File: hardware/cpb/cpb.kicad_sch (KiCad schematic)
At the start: 132 parts, among them J1 Spacecraft Bus Stacking Conne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, J10 SW1, J11 SW2, J12 SW3, J13 PISW1, J14 μSW1, J15 μSW2, J16 μSW3, J17 μSW4, J2 I2CExt, J3 DAC1BUF, J4 DAC2BUF, J6 Raspberry Pi Zero 2W, J7 ADC6/7, J8 ADC2/3, J9 4FBRG, J99 RBFJUMP, Q1 PMBT2222A, Q2 IRF9393, Q3 MBT2222ADW1T1, Q4 PMBT2222A, U1 TS912, U2 ADR420ARMZ, U3 KF33BDT, U4 STM32L072R_B-Z_Tx, U5 AP62301WU, U6 SC16IS750xBS, Y1 14.7456MHz

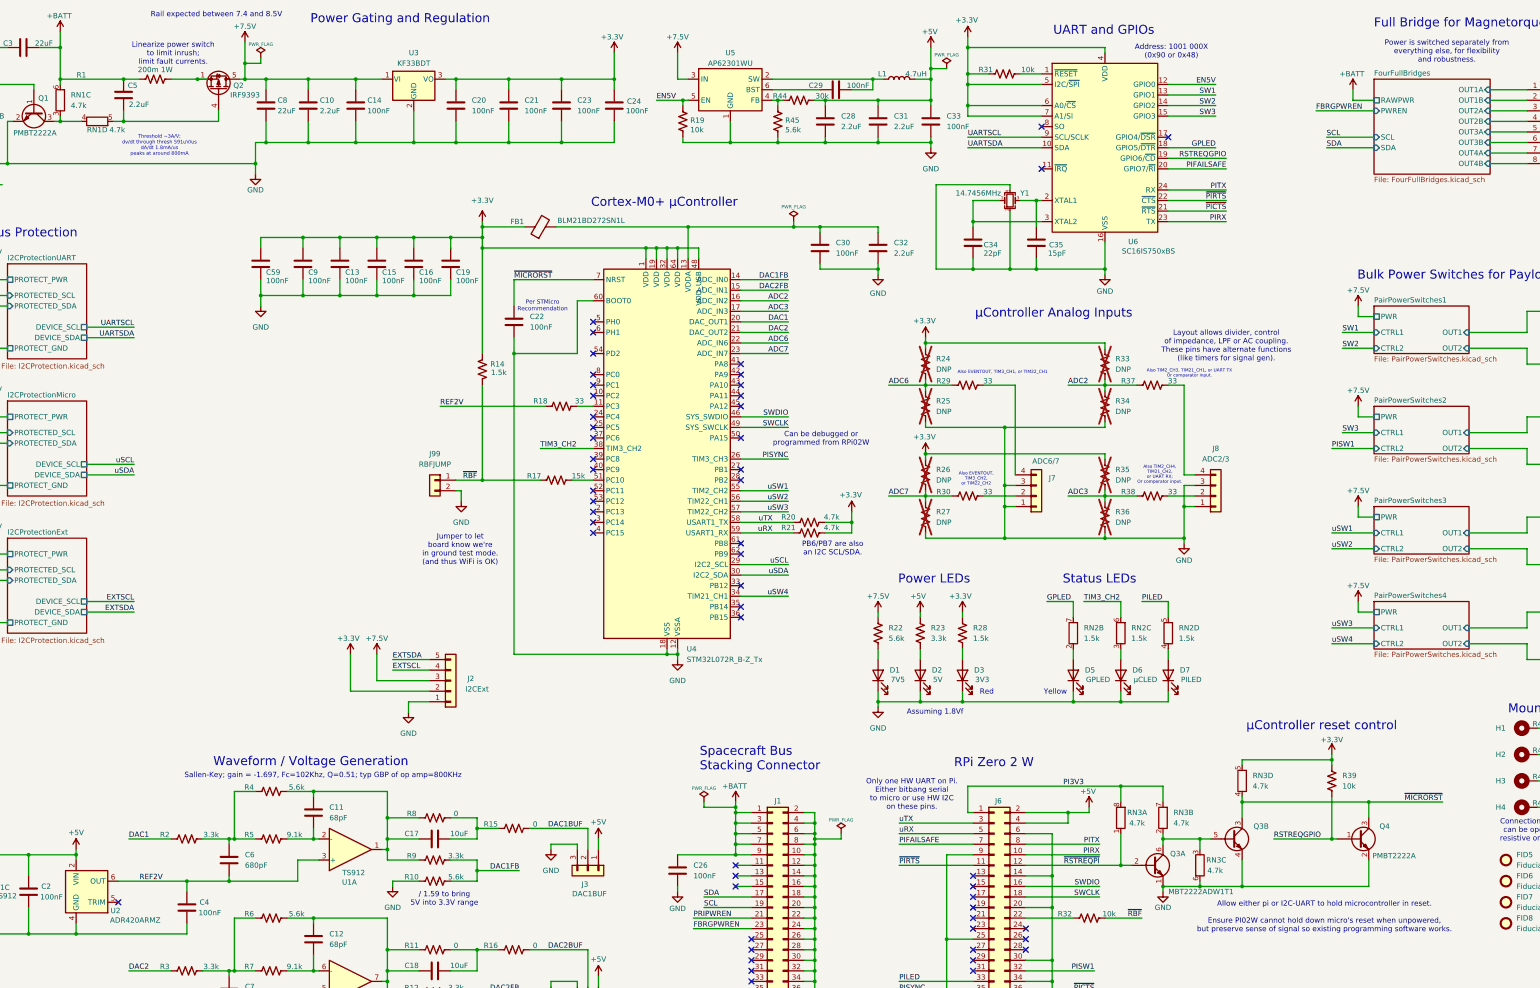
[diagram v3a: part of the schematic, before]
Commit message: hardware/cpb: finished revisions
did all things specified on Errata file for cpb;
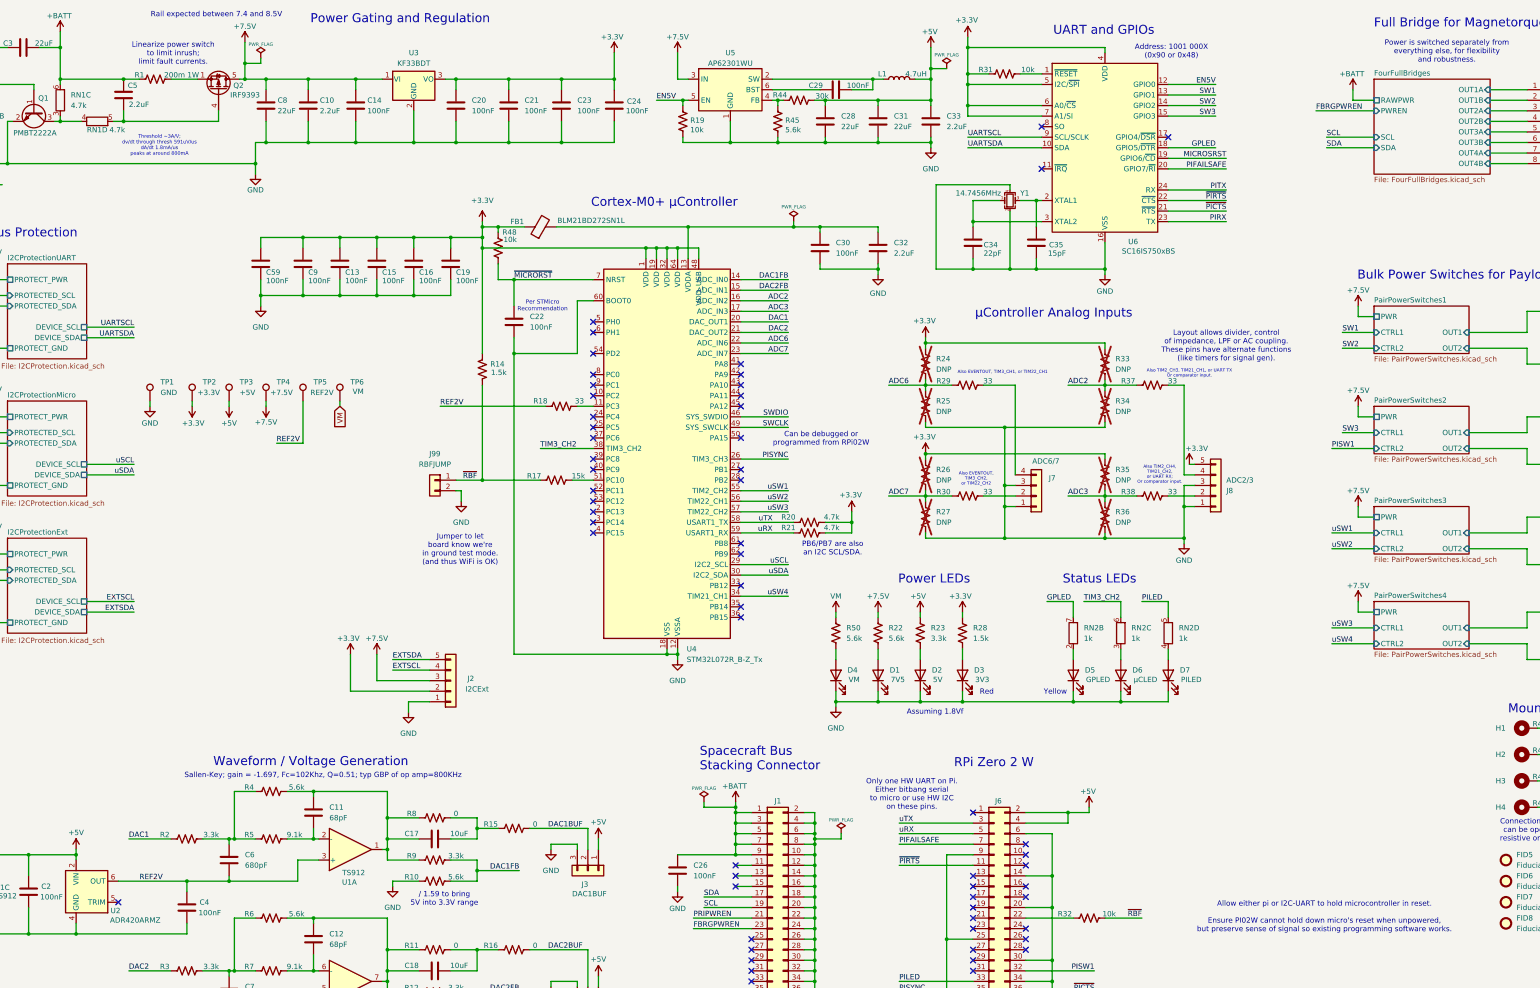
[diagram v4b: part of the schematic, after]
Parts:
- removed J8: ADC2/3, Connector_JST:JST_PH_B4B-PH-K_1x04_P2.00mm_Vertical, symbol Connector_Generic:Conn_01x04
- removed Q3: MBT2222ADW1T1, Package_TO_SOT_SMD:SOT-363_SC-70-6, symbol Transistor_BJT:MBT2222ADW1T1
- removed Q4: PMBT2222A, Package_TO_SOT_SMD:SOT-23, symbol Transistor_BJT:PMBT2222A
- removed R39: 10k, Resistor_SMD:R_0603_1608Metric, symbol Device:R_US
- removed RN3: 4.7k, Resistor_SMD:R_Array_Convex_4x0603, symbol Device:R_Pack04_Split
- added D4: VM, LED_SMD:LED_0805_2012Metric, symbol Device:LED
- added J8: ADC2/3, symbol Connector_Generic:Conn_01x05
- added R48: 10k, symbol Device:R_US
- added R50: 5.6k, Resistor_SMD:R_0603_1608Metric, symbol Device:R_US
- added TP1: GND, TestPoint:TestPoint_Keystone_5010-5014_Multipurpose, symbol Connector:TestPoint
- added TP2: +3.3V, TestPoint:TestPoint_Keystone_5010-5014_Multipurpose, symbol Connector:TestPoint
- added TP3: +5V, TestPoint:TestPoint_Keystone_5010-5014_Multipurpose, symbol Connector:TestPoint
- added TP4: +7.5V, TestPoint:TestPoint_Keystone_5010-5014_Multipurpose, symbol Connector:TestPoint
- added TP5: REF2V, TestPoint:TestPoint_Keystone_5010-5014_Multipurpose, symbol Connector:TestPoint
- added TP6: VM, TestPoint:TestPoint_Keystone_5010-5014_Multipurpose, symbol Connector:TestPoint
- C28, C31: value 2.2uF -> 22uF; LCSC C77047 -> C2178186
- C33: value 100nF -> 2.2uF; LCSC C77055 -> C77047
- RN2: value 1.5k -> 1k; LCSC C723702 -> C22548
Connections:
- net +3.3V: now also J8.5 (Pin_5), R48.1, TP2.1
- net +5V: now also TP3.1
- net +7.5V: now also TP4.1
- net GND: now also D4.1 (K), J8.1 (Pin_1), J8.3 (Pin_3), TP1.1
- net PIRX: no longer J6.10 (Pin_10)
- net PITX: no longer J6.8 (Pin_8)
- net REF2V: now also TP5.1
- net SWCLK: no longer J6.18 (Pin_18)
- net SWDIO: no longer J6.16 (Pin_16)
- net ~{MICRORST}: now also R48.2
- net at R38.2: now also J8.2 (Pin_2)
- net at R37.2: now also J8.4 (Pin_4)
- net PI3V3: no longer names the net of J6.1 (Pin_1)
- net RSTREQGPIO renamed MICROSRST
- net ~{RSTREQPI}: no longer names the net of J6.12 (Pin_12)
- new net: D4.2 (A), R50.2
- new net VM: R50.1, TP6.1
- no-connect marks 57 -> 63
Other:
- note removed: "μController reset control"

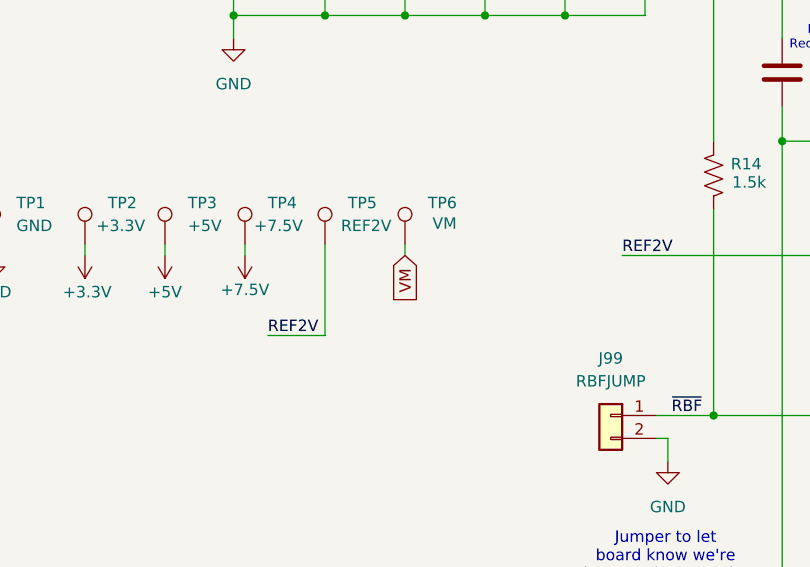
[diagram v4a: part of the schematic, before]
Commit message: hardware/cpb: changed labels, spread out components
changed vm labels, spread out somponents on Four Full Bridges sch;
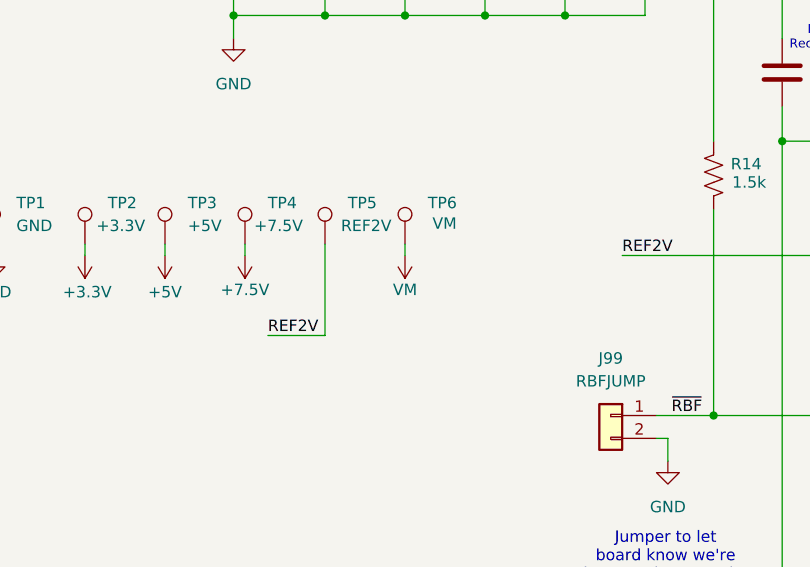
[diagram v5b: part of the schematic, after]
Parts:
- R48: footprint (none) -> Resistor_SMD:R_0603_1608Metric
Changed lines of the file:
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@@
 		)
 	)
-	(global_label "VM"
-		(shape input)
-		(at 111.76 107.95 270)
-		(fields_autoplaced yes)
-		(effects
-			(font
-				(size 1.27 1.27)
-			)
-			(justify right)
-		)
-		(property "Intersheetrefs" "${INTERSHEET_REFS}"
-			(at 111.76 113.4752 90)
-			(effects
-				(font
-					(size 1.27 1.27)
-				)
-				(justify right)
-				(hide yes)
-			)
-		)
-	)
 	(symbol
 		(lib_id "Device:C")
@@
 	)
 	(symbol
+		(lib_id "power:+7.5V")
+		(at 111.76 107.95 180)
+		(unit 1)
+		(exclude_from_sim no)
+		(in_bom yes)
+		(on_board yes)
+		(dnp no)
+		(property "Reference" "#PWR081"
+			(at 111.76 104.14 0)
+			(effects
+				(font
+					(size 1.27 1.27)
+				)
+				(hide yes)
+			)
+		)
+		(property "Value" "VM"
+			(at 111.76 111.76 0)
+			(effects
+				(font
+					(size 1.27 1.27)
+				)
+			)
+		)
+		(property "Footprint" ""
+			(at 111.76 107.95 0)
+			(effects
+				(font
+					(size 1.27 1.27)
+				)
+				(hide yes)
+			)
+		)
+		(property "Datasheet" ""
+			(at 111.76 107.95 0)
+			(effects
+				(font
+					(size 1.27 1.27)
+				)
+				(hide yes)
+			)
+		)
+		(property "Description" "Power symbol creates a global label with name \"+7.5V\""
+			(at 111.76 107.95 0)
+			(effects
+				(font
+					(size 1.27 1.27)
+				)
+				(hide yes)
+			)
+		)
+		(pin "1"
+		)
+		(instances
+			(project "cpb"
+				(path "/9a10a1ee-db5a-47ad-90f3-81b92d74d449"
+					(reference "#PWR081")
+					(unit 1)
+				)
+			)
+		)
+	)
+	(symbol
 		(lib_id "Device:R_Pack04_Split")
 		(at 44.45 34.29 0)
@@
 			)
 		)
-		(property "Footprint" ""
+		(property "Footprint" "Resistor_SMD:R_0603_1608Metric"
 			(at 150.876 70.104 90)
 			(effects

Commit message: hardware/cpb: fixed BOM issues and placed new components down.
C28 and C31 were given an 0805 footprint, J8 was given a footprint, placed testpoints and new LED.
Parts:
- C28, C31: footprint Capacitor_SMD:C_0603_1608Metric -> Capacitor_SMD:C_0805_2012Metric
- J8: footprint (none) -> Connector_JST:JST_PH_B5B-PH-K_1x05_P2.00mm_Vertical
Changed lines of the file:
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@@
 			)
 		)
-		(property "Footprint" ""
+		(property "Footprint" "Connector_JST:JST_PH_B5B-PH-K_1x05_P2.00mm_Vertical"
 			(at 322.58 127 0)
 			(effects
@@
 			)
 		)
-		(property "Footprint" "Capacitor_SMD:C_0603_1608Metric"
+		(property "Footprint" "Capacitor_SMD:C_0805_2012Metric"
 			(at 242.2652 43.18 0)
 			(effects
@@
 			)
 		)
-		(property "Footprint" "Capacitor_SMD:C_0603_1608Metric"
+		(property "Footprint" "Capacitor_SMD:C_0805_2012Metric"
 			(at 229.5652 43.18 0)
 			(effects

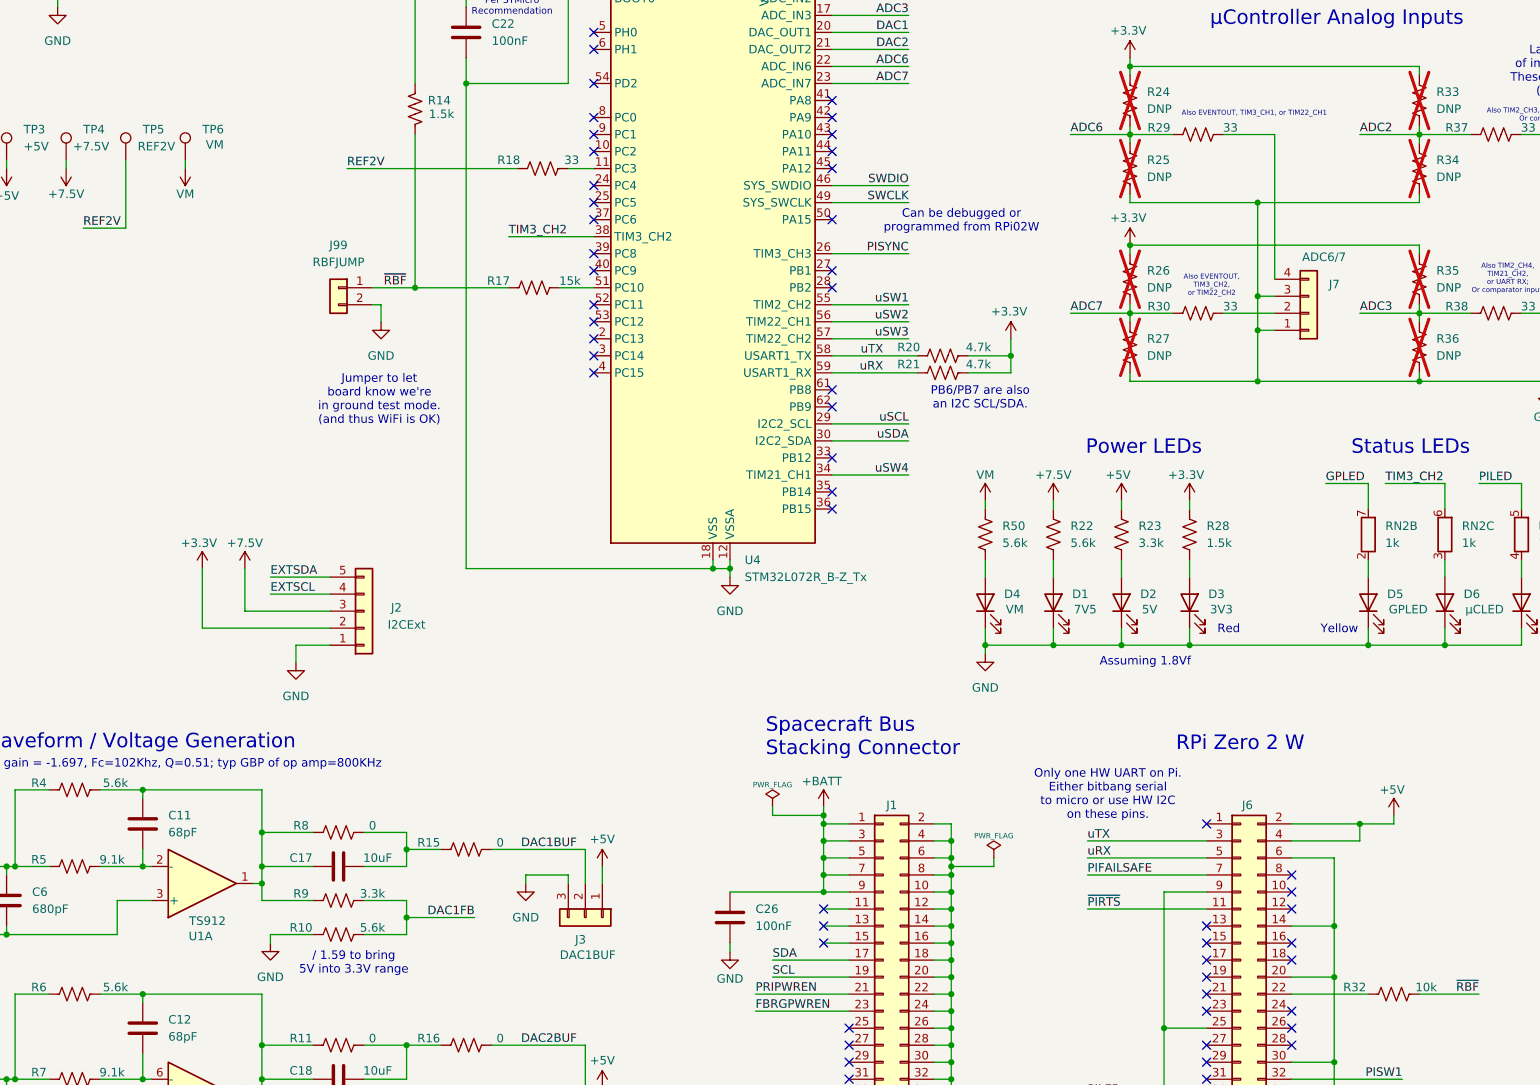
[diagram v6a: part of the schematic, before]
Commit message: hardware/cpb: J7 changed to 5 pin.
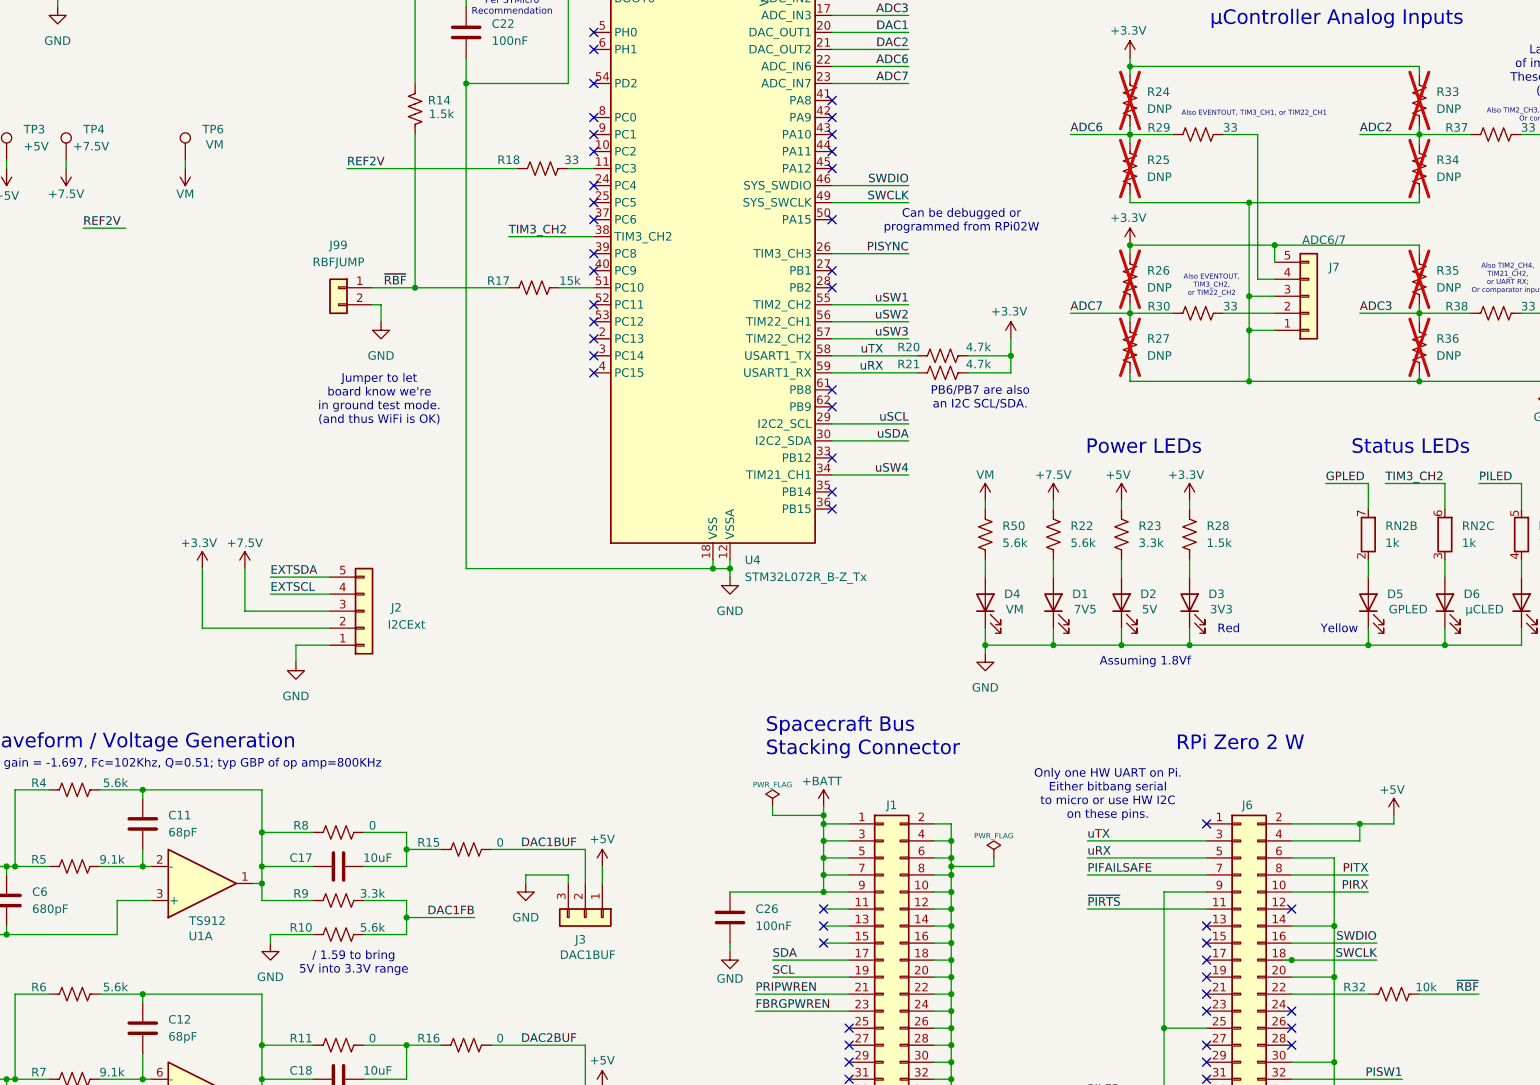
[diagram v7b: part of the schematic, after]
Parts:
- removed TP5: REF2V, TestPoint:TestPoint_Keystone_5010-5014_Multipurpose, symbol Connector:TestPoint
- J7: footprint Connector_JST:JST_PH_B4B-PH-K_1x04_P2.00mm_Vertical -> Connector_JST:JST_PH_B5B-PH-K_1x05_P2.00mm_Vertical; symbol Connector_Generic:Conn_01x04 -> Connector_Generic:Conn_01x05
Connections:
- net +3.3V: now also J7.5 (Pin_5)
- net PIRX: now also J6.10 (Pin_10)
- net PITX: now also J6.8 (Pin_8)
- net SWCLK: now also J6.18 (Pin_18)
- net SWDIO: now also J6.16 (Pin_16)
- no-connect marks 63 -> 59
